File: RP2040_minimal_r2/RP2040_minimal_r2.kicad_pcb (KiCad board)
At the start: 2 copper layers, 46 x 34 mm, 36 parts, among them J1 SPI0.6, J2 SPI0.8, J3 SPI1.13, J4 I2C0, J5 USB, SW1 BOOT, SW2 RESET, U1 AP2112K-3.3TRG1, U2 W25Q128JVS, U3 RP2040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

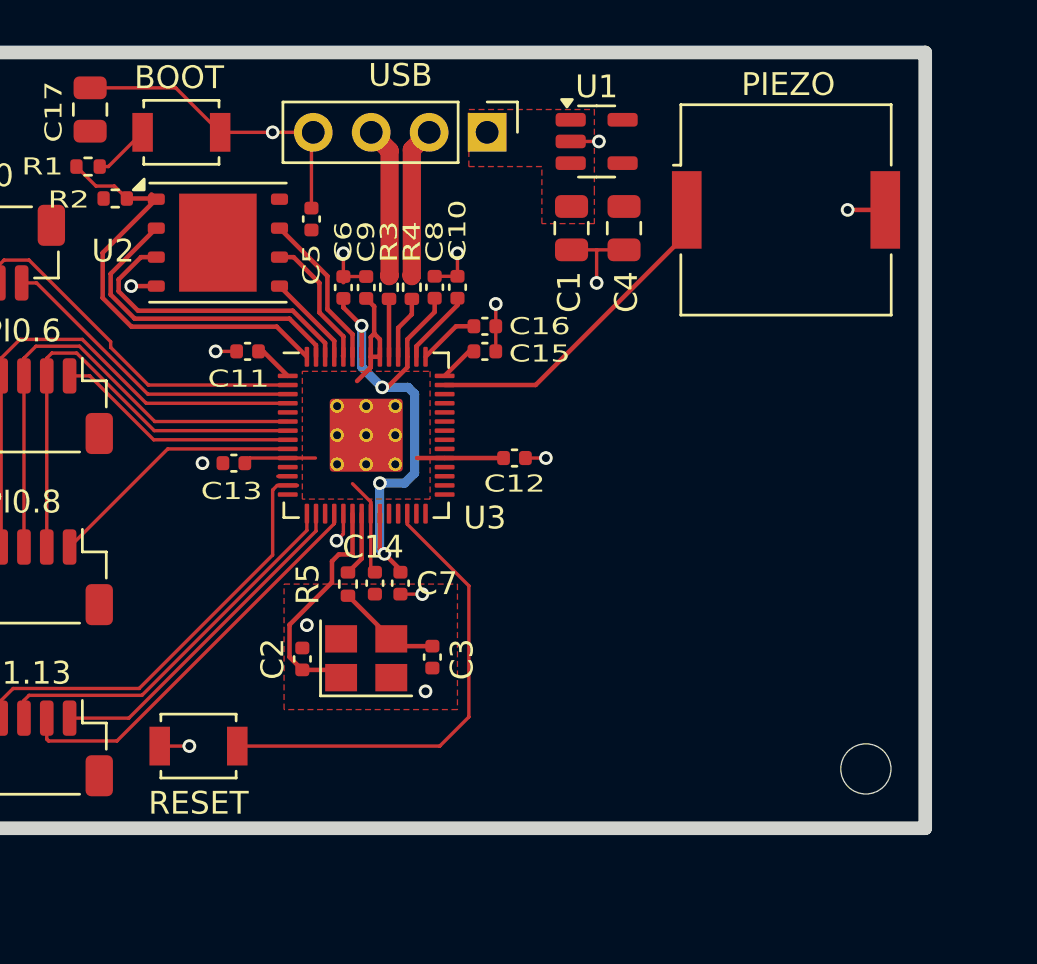
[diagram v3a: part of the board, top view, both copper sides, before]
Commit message: Added 6 button connectors. Added 6 pin breakout for GPIO 26-29 (includes ground and +3.3v as well).
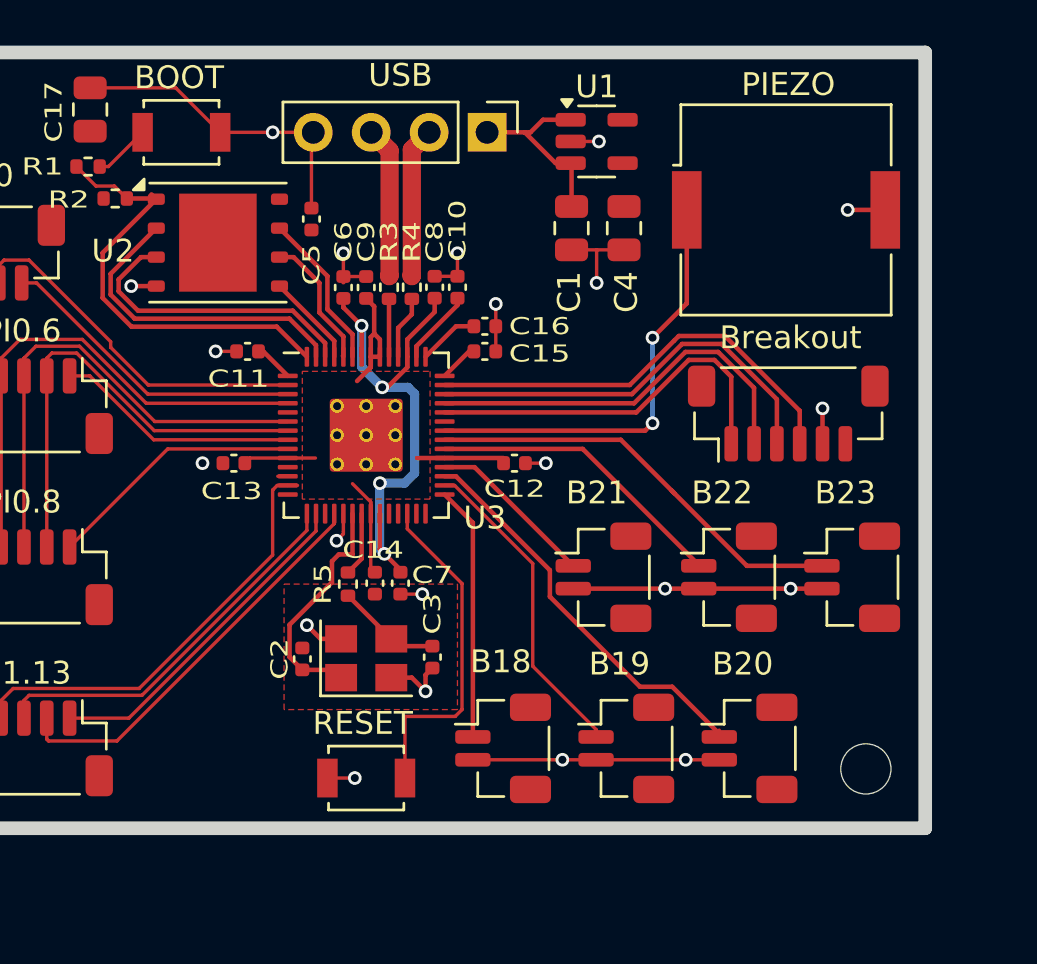
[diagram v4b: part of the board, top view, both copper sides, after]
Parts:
- added J10: B22, Connector_JST:JST_SH_BM02B-SRSS-TB_1x02-1MP_P1.00mm_Vertical, F.Cu at (114.4, 93.0)
- added J11: B23, Connector_JST:JST_SH_BM02B-SRSS-TB_1x02-1MP_P1.00mm_Vertical, F.Cu at (119.8, 93.0)
- added J12: Breakout, Connector_JST:JST_SH_BM06B-SRSS-TB_1x06-1MP_P1.00mm_Vertical, F.Cu at (117.0, 85.8)
- added J6: B18, Connector_JST:JST_SH_BM02B-SRSS-TB_1x02-1MP_P1.00mm_Vertical, F.Cu at (104.5, 100.5)
- added J7: B19, Connector_JST:JST_SH_BM02B-SRSS-TB_1x02-1MP_P1.00mm_Vertical, F.Cu at (109.9, 100.5)
- added J8: B20, Connector_JST:JST_SH_BM02B-SRSS-TB_1x02-1MP_P1.00mm_Vertical, F.Cu at (115.3, 100.5)
- added J9: B21, Connector_JST:JST_SH_BM02B-SRSS-TB_1x02-1MP_P1.00mm_Vertical, F.Cu at (108.9, 93.0)
- moved SW2 7.48 mm to (98.5, 101.8)
- moved C12 0.22 mm to (105.0, 88.0)
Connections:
- U3 pad 29: unconnected-(U3-GPIO18-Pad29) -> GPIO18
- U3 pad 30: unconnected-(U3-GPIO19-Pad30) -> GPIO19
- U3 pad 31: unconnected-(U3-GPIO20-Pad31) -> GPIO20
- U3 pad 32: unconnected-(U3-GPIO21-Pad32) -> GPIO21
- U3 pad 34: unconnected-(U3-GPIO22-Pad34) -> GPIO22
- U3 pad 35: unconnected-(U3-GPIO23-Pad35) -> GPIO23
- U3 pad 36: unconnected-(U3-GPIO24-Pad36) -> /PIEZO
- U3 pad 38: unconnected-(U3-GPIO26_ADC0-Pad38) -> GPIO26
- U3 pad 39: unconnected-(U3-GPIO27_ADC1-Pad39) -> GPIO27
- U3 pad 40: unconnected-(U3-GPIO28_ADC2-Pad40) -> GPIO28
- U3 pad 41: /PIEZO -> GPIO29
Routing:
- net GND: track 53.3 -> 81.1 mm, vias 18 -> 23
- net GPIO29: track 0.00 -> 19.3 mm
- net GPIO23: track 0.00 -> 19.0 mm
- net GPIO28: track 0.00 -> 18.4 mm
- net GPIO20: track 0.00 -> 17.8 mm
- net GPIO27: track 0.00 -> 17.6 mm
- net GPIO26: track 0.00 -> 16.8 mm
- net GPIO19: track 0.00 -> 14.0 mm
- net GPIO22: track 0.00 -> 13.3 mm
- net GPIO18: track 0.00 -> 11.1 mm
- net VBUS: track 0.00 -> 8.38 mm
- net GPIO21: track 0.00 -> 7.43 mm
- net /RUN: track 20.7 -> 14.9 mm
- net /PIEZO: track 14.4 -> 19.3 mm, vias 0 -> 2
- removed copper zone on F.Cu, net VBUS

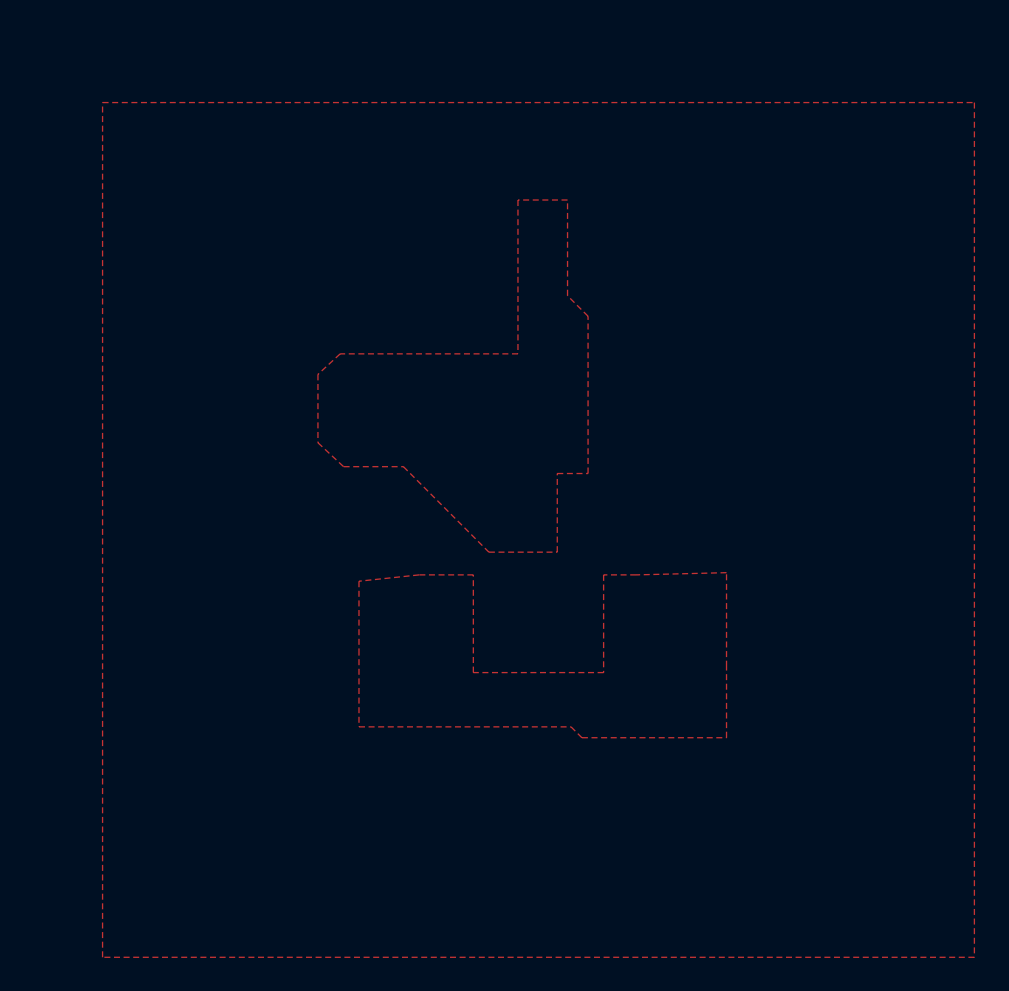
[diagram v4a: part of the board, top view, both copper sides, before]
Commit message: Update gerbers and BOM/placement files. Add readme file. Add github url to rear silkscreen layer. Clean up some old unused fill zones that I'd moved off to the side.
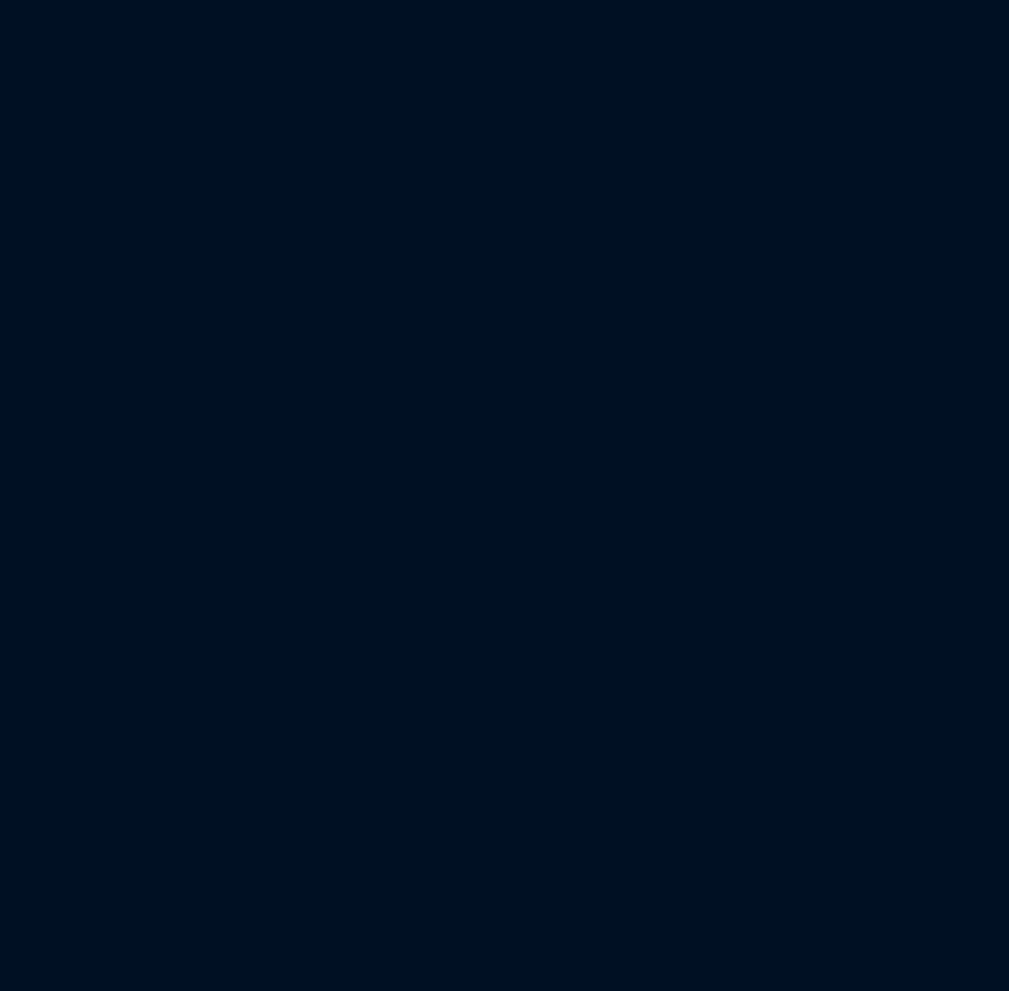
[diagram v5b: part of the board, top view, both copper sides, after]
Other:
- board text added: "https://github.com/monroewilliams/RP2040_trackball"
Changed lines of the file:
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@@
 			(viasonmask no)
 			(mode 1)
-			(useauxorigin no)
+			(useauxorigin yes)
 			(hpglpennumber 1)
 			(hpglpenspeed 20)
@@
 			)
 		)
-		(property "LCSC" "C97521"
+		(property "LCSC" "C190862"
 			(at 0 0 0)
 			(unlocked yes)
@@
 			)
 		)
-		(property "LCSC" "C271750"
+		(property "LCSC" "C231329"
 			(at 0 0 0)
 			(unlocked yes)
@@
 			)
 		)
-		(property "LCSC" "C271750"
+		(property "LCSC" "C231329"
 			(at 0 0 180)
 			(unlocked yes)
@@
 			)
 		)
+		(property "LCSC" "C160388"
+			(at 0 0 -90)
+			(unlocked yes)
+			(layer "F.Fab")
+			(hide yes)
+			(effects
+				(font
+					(size 1 1)
+					(thickness 0.15)
+				)
+			)
+		)
 		(property ki_fp_filters "Connector*:*_1x??_*")
 		(sheetname "Root")
@@
 			)
 		)
+		(property "LCSC" "C160388"
+			(at 0 0 -90)
+			(unlocked yes)
+			(layer "F.Fab")
+			(hide yes)
+			(effects
+				(font
+					(size 1 1)
+					(thickness 0.15)
+				)
+			)
+		)
 		(property ki_fp_filters "Connector*:*_1x??_*")
 		(sheetname "Root")
@@
 		(tags "connector JST SH vertical")
 		(property "Reference" "J4"
-			(at 0 -3.3 360)
+			(at 0 -3.3 0)
 			(layer "F.SilkS")
 			(hide yes)
@@
 		)
 		(property "Value" "I2C0"
-			(at -0.4 -3.375 360)
+			(at -0.4 -3.375 0)
 			(layer "F.SilkS")
 			(effects
@@
 			)
 		)
+		(property "LCSC" "C160390"
+			(at 0 0 0)
+			(unlocked yes)
+			(layer "F.Fab")
+			(hide yes)
+			(effects
+				(font
+					(size 1 1)
+					(thickness 0.15)
+				)
+			)
+		)
 		(property ki_fp_filters "Connector*:*_1x??_*")
 		(sheetname "Root")
@@
 		)
 		(fp_text user "${REFERENCE}"
-			(at 0 -0.25 360)
+			(at 0 -0.25 0)
 			(layer "F.Fab")
 			(effects
@@
 		(sheetname "Root")
 		(sheetfile "RP2040_minimal_r2.kicad_sch")
-		(attr through_hole)
+		(attr through_hole dnp)
 		(fp_line
 			(start -1.33 8.95)
@@
 			)
 		)
+		(property "LCSC" "C160388"
+			(at 0 0 -90)
+			(unlocked yes)
+			(layer "F.Fab")
+			(hide yes)
+			(effects
+				(font
+					(size 1 1)
+					(thickness 0.15)
+				)
+			)
+		)
 		(property ki_fp_filters "Connector*:*_1x??_*")
 		(sheetname "Root")
@@
 		(tags "connector JST SH vertical")
 		(property "Reference" "J7"
-			(at 0 -3.3 360)
+			(at 0 -3.3 0)
 			(layer "F.SilkS")
 			(hide yes)
@@
 			)
 		)
+		(property "LCSC" "C160388"
+			(at 0 0 -90)
+			(unlocked yes)
+			(layer "F.Fab")
+			(hide yes)
+			(effects
+				(font
+					(size 1 1)
+					(thickness 0.15)
+				)
+			)
+		)
 		(property ki_fp_filters "Connector*:*_1x??_*")
 		(sheetname "Root")
@@
 			)
 		)
+		(property "LCSC" "C160388"
+			(at 0 0 -90)
+			(unlocked yes)
+			(layer "F.Fab")
+			(hide yes)
+			(effects
+				(font
+					(size 1 1)
+					(thickness 0.15)
+				)
+			)
+		)
 		(property ki_fp_filters "Connector*:*_1x??_*")
 		(sheetname "Root")
@@
 			)
 		)
+		(property "LCSC" "C160388"
+			(at 0 0 -90)
+			(unlocked yes)
+			(layer "F.Fab")
+			(hide yes)
+			(effects
+				(font
+					(size 1 1)
+					(thickness 0.15)
+				)
+			)
+		)
 		(property ki_fp_filters "Connector*:*_1x??_*")
 		(sheetname "Root")
@@
 		(layer "Edge.Cuts")
 	)
+	(gr_text "https://github.com/monroewilliams/RP2040_trackball"
+		(at 120.8 77.9 0)
+		(layer "B.SilkS")
+		(effects
+			(font
+				(size 1 1)
+				(thickness 0.15)
+			)
+			(justify left bottom mirror)
+		)
+	)
 	(segment
 		(start 92.1 73.5)
@@
 			)
 		)
-	)
-	(zone
-		(net 5)
-		(net_name "+3V3")
-		(layer "F.Cu")
-		(hatch edge 0.508)
-		(connect_pads
-			(clearance 0.25)
-		)
-		(min_thickness 0.2)
-		(filled_areas_thickness no)
-		(fill yes
-			(thermal_gap 0.3)
-			(thermal_bridge_width 0.3)
-		)
-		(polygon
-			(pts
-				(xy 193.684924 127.721696) (xy 142.684924 127.721696) (xy 142.684924 77.721696) (xy 193.684924 77.721696)
-			)
-		)
-		(polygon
-			(pts
-				(xy 179.184924 105.221696) (xy 173.899924 105.351696) (xy 171.994924 105.351696) (xy 171.994924 111.066696)
-				(xy 164.374924 111.066696) (xy 164.374924 105.351696) (xy 161.199924 105.351696) (xy 157.684924 105.721696)
-				(xy 157.684924 109.721696) (xy 157.684924 114.241696) (xy 170.089924 114.241696) (xy 170.724924 114.876696)
-				(xy 179.184924 114.876696) (xy 179.184924 110.721696)
-			)
-		)
-		(polygon
-			(pts
-				(xy 166.984924 83.421696) (xy 166.984924 92.421696) (xy 156.584924 92.421696) (xy 155.284924 93.621696)
-				(xy 155.284924 97.621696) (xy 156.784924 99.021696) (xy 160.284924 99.021696) (xy 165.284924 104.021696)
-				(xy 169.284924 104.021696) (xy 169.284924 99.421696) (xy 171.084924 99.421696) (xy 171.084924 90.221696)
-				(xy 169.884924 89.021696) (xy 169.884924 83.421696)
-			)
-		)

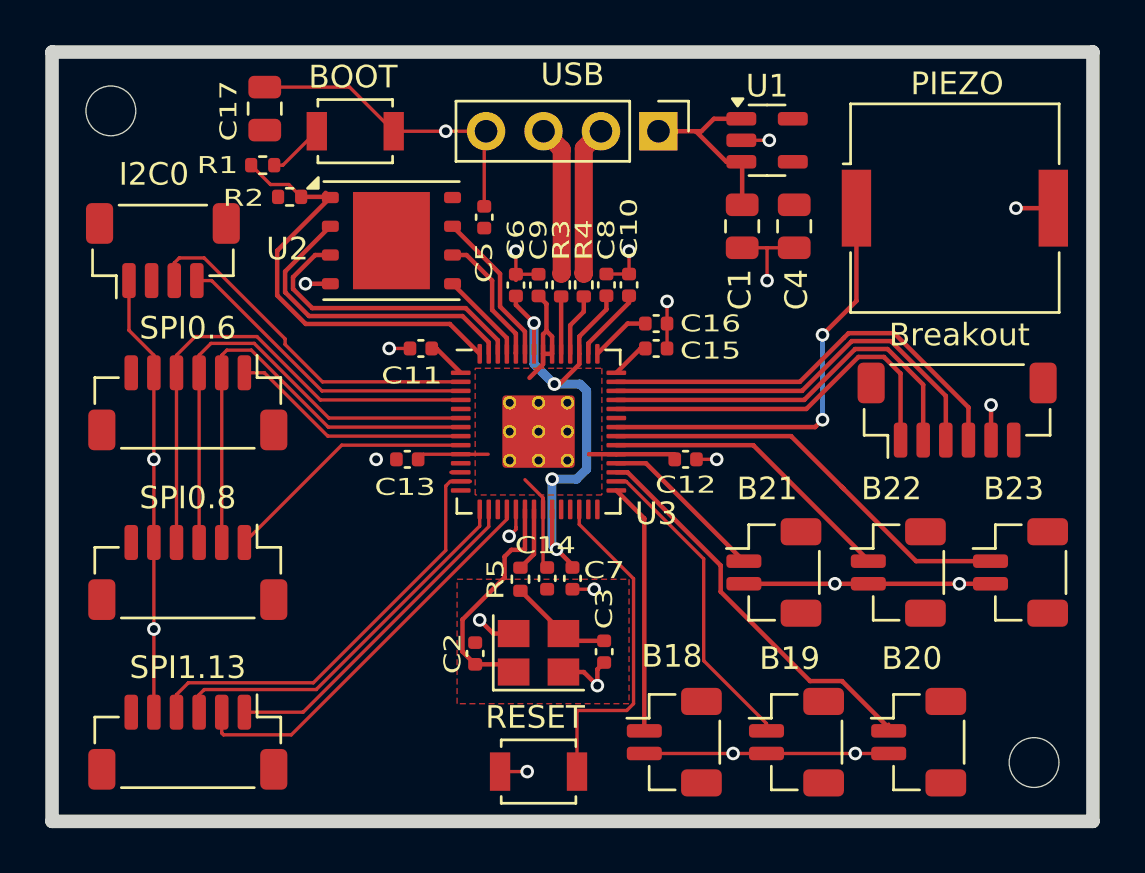
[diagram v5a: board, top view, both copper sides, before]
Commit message: Added a WS2812 LED (a.k.a. NeoPixel) Removed some top-side ground traces in favor of vias closer to ground pads. Updated the github URL. Minor changes to the readme.
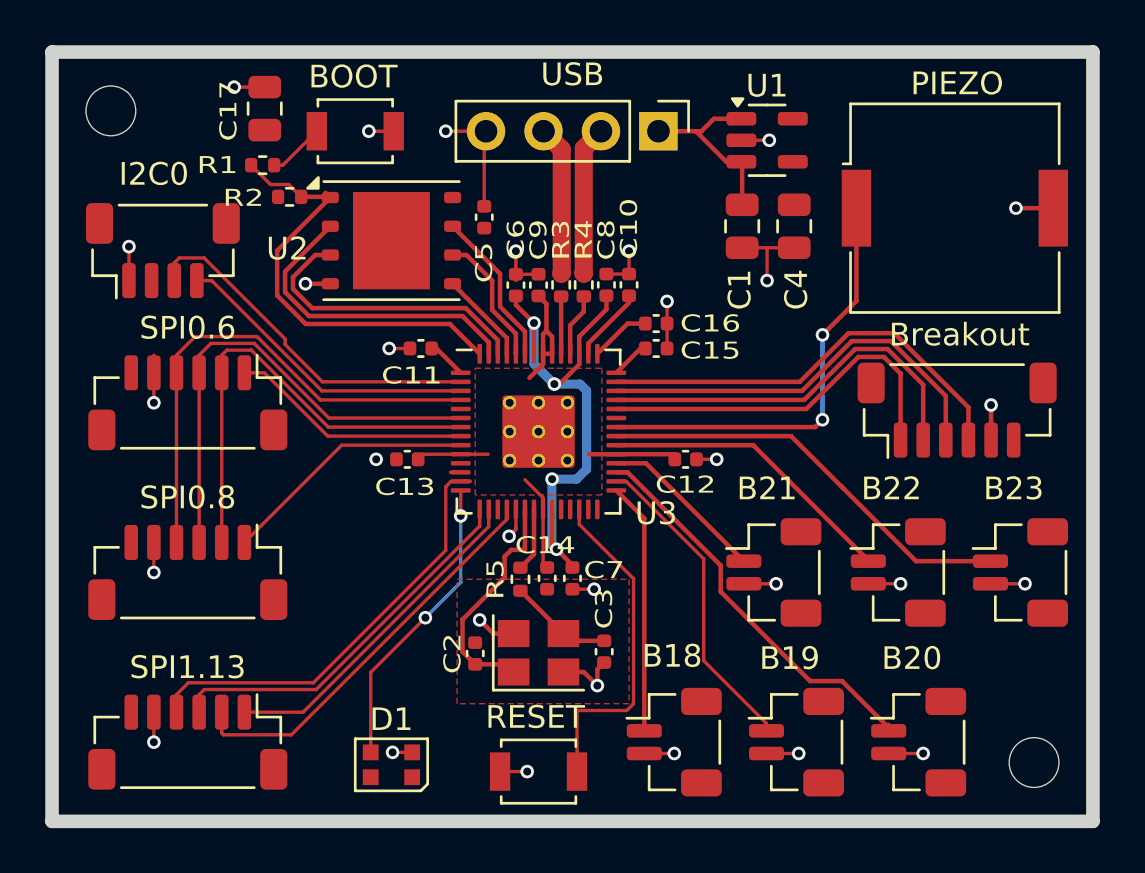
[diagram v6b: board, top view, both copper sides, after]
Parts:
- added D1: WS2812B-2020, LED_SMD:LED_WS2812B-2020_PLCC4_2.0x2.0mm, F.Cu at (92.0, 101.5)
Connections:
- U3 pad 14: unconnected-(U3-GPIO11-Pad14) -> /NEOPIXEL
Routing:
- net GND: track 81.1 -> 49.2 mm, vias 23 -> 30
- net /NEOPIXEL: track 0.00 -> 13.3 mm, vias 0 -> 2
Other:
- board text added: "https://github.com/monroewilliams/rp2040_mwtrackball"
- board text removed: "https://github.com/monroewilliams/RP2040_trackball"
